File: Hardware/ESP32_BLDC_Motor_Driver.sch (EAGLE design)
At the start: 125 parts, among them J1 USB-C Connector, J2 0532610371, J3 POWER_JACKPOWER_JACK_SLOT, J4 Breadboard Connector, J5 Breadboard Headers, J6 0.1in header, J7 QWIIC_RIGHT_ANGLE, J8 Breakout Header, Q1 20V/4.2A/52mΩ/1.4W, Q2 NPN Transistors, U1 TMC6300, U3 ESP-WROOM-3232D, U4 CH340C, U5 ESD Diode, U6 AP63357, U7 AP2202-ADJ, U8 TMAG5273, U9 LMV324

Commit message: Design review changes
Updated datasheets with correct parts in it now; removed power jack; changed direction of motor and output connector to the motor; swapped resistances of op amp for inline current sensing; updated sizes of some resistances; fixed power scheme of the board; added perfect diode circuit; for more information, see protos review doc
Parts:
- removed C16: 10uF, SparkFun-Capacitors:10UF-0603-6.3V-20%
- removed C20, C21: 22uF, SparkFun-Capacitors:22UF-0603-6.3V-20%
- removed D1: 1A/40V/500mV, SparkFun-DiscreteSemi:DIODE-SCHOTTKY-SS14
- removed J2: 0532610371, 0532610371:0532610371
- removed J3: POWER_JACKPOWER_JACK_SLOT, SparkFun-Connectors:POWER_JACKPOWER_JACK_SLOT
- removed J6: 0.1in header, SparkFun-Connectors:CONN_03
- removed J8: Breakout Header, SparkFun-Connectors:CONN_02
- removed L1: 4.7μH, SparkFun-Coils:4.7μH_SHIELDED_INDUCTORNPIS_LS
- removed MOTOR: JUMPER-SMT_2_NC_TRACE_SILK, SparkFun-Jumpers:JUMPER-SMT_2_NC_TRACE_SILK
- removed MPWR: RED, SparkFun-LED:LED-RED_0603-KB
- removed R22: 16.2k, SparkFun-Resistors:16.2KOHM-0603-1/10W-1%
- removed R23: 26.7k, SparkFun-Resistors:26.7KOHM0603-1/10W-1%
- removed R5: 93.1k, SparkFun-Resistors:93.1KOHM
- removed R6: 30.1k, SparkFun-Resistors:30.1KOHM-0603-1/10W-1%
- removed U6: AP63357, SparkFun-IC-Power:AP63357
- removed U7: AP2202-ADJ, SparkFun-IC-Power:AP2202-ADJ
- added C12: 0.1uF, SparkFun-Capacitors:0.1UF-0603-25V-(+80/-20%)
- added MEAS: JUMPER-COMBO_2_NC_TRACE, SparkFun-Jumpers:JUMPER-COMBO_2_NC_TRACE
- added P1: 0532610371, 0532610371:0532610371
- added Q3: 20V/4.2A/52mΩ/1.4W, SparkFun-DiscreteSemi:MOSFET_PCH-DMG2305UX-7
- added U2: 3.3V, SparkFun-IC-Power:V_REG_AP2112K-3.3V
- C11: value 100pF -> 0.1uF; device SparkFun-Capacitors:100PF-0603-50V-5% -> SparkFun-Capacitors:0.1UF-0603-25V-(+80/-20%)
- C5: value 0.1uF -> 10nF; device SparkFun-Capacitors:0.1UF-0603-25V-(+80/-20%) -> SparkFun-Capacitors:10NF-0603-50V-10%
- C6: value 33pF -> 0.1uF; device SparkFun-Capacitors:33PF-0603-50V-5% -> SparkFun-Capacitors:0.1UF-0603-25V-(+80/-20%)
- C7: device SparkFun-Capacitors:10UF-0603-6.3V-20% -> SparkFun-Capacitors:10UF-POLAR-0603-6.3V-20%(TANT)
- Q1: value 20V/4.2A/52mΩ/1.4W -> (none); device SparkFun-DiscreteSemi:MOSFET_PCH-DMG2305UX-7 -> SparkFun-DiscreteSemi:TRANS_PNP_DUALSOT-363
- R1: value 4.7k -> 100k; device SparkFun-Resistors:4.7KOHM-0603-1/10W-1% -> SparkFun-Resistors:100KOHM-0603-1/10W-1%
- R4: value 100k -> 1M; device SparkFun-Resistors:100KOHM-0603-1/10W-1% -> SparkFun-Resistors:1MOHM-0603-1/4W-5%
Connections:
- removed net 3.3V_A: C1.1, C17.1, C22.1, C4.1, C9.1, J7.2, PWR.2, R16.2, R22.2, STAT.VCC, U3.3V3, U4.V3, U4.VCC, U7.OUT
- removed net 3.3V_PG: J5.1, U6.PG
- removed net BST: C5.1, U6.BST
- removed net ESP_13/U_OUT: R35.2, TP10.1, U3.PICO2/IOA13, U9G2.OUT
- removed net ESP_14/DIAG: D.2, U1.DIAG, U3.SCK2/IOA14
- removed net ESP_34/AUX1: J5.7, S3.1, S3.2, U3.IA34
- removed net ESP_35/AUX2: J5.8, S4.1, S4.2, U3.IA35
- removed net FB: C6.2, R5.1, R6.2, U6.FB
- removed net LDO_EN: R24.1, U7.EN
- removed net MOTOR_EN: J4.6, U6.EN
- removed net N$23: MOTOR.1, R1.2
- removed net N$34: MPWR.A, R1.1
- removed net N$5: J3.GNDBREAK, Q1.G, R4.1
- removed net POWER_IN: D1.A, J3.PWR
- removed net SW: C5.2, L1.1, U6.SW
- removed net VIN: C10.1, C16.1, C7.1, D1.C, J8.2, Q1.S, R24.2, R4.2, U6.VIN, U7.IN
- new net 5V: BYP.2, C10.1, C12.1, F1.2, R24.2, U2.IN
- new net 5V_MEAS: MEAS.1, Q1G2.E, Q3.S
- new net ESP_13/AUX2: J5.8, S4.1, S4.2, U3.PICO2/IOA13
- new net ESP_14/AUX1: J5.7, S3.1, S3.2, U3.SCK2/IOA14
- new net ESP_21/TP_SDA1: R27.1
- new net ESP_34/DIAG: D.2, U1.DIAG, U3.IA34
- new net ESP_35/U_OUT: R29.2, TP10.1, U3.IA35, U9G2.OUT
- new net N$21: Q1G2.C, Q3.G, R4.2
- new net N$22: Q1G1.B, Q1G1.E, Q1G2.B, R1.2
- new net N$6: R24.1, U2.EN
- net 3.3V: now also C1.1, C17.1, C22.1, C4.1, C9.1, J7.2, PWR.2, R16.2, STAT.VCC, U2.OUT, U3.3V3, U4.VCC; no longer C20.1, C21.1, C6.1, L1.2, MOTOR.2, R5.2
- net ESP_21/TP_SDA: now also J4.3; no longer J4.2, R27.1
- net ESP_22/TP_SCL: now also J4.2; no longer J4.1
- net ESP_25/TP_A1: now also J4.6; no longer J4.5
- net ESP_26/TP_A0: now also J4.5; no longer J4.4
- net ESP_27/GPIO2: now also J4.4; no longer J4.3
- net ESP_36/V_OUT: now also R40.2; no longer R36.2
- net ESP_39/W_OUT: now also R41.2; no longer R37.2
- net GND: now also C12.2, C5.2, C6.2, C7.-, J4.1, J5.1, R1.1, R30.2, R4.1, R42.2, R43.2, U2.GND; no longer C16.2, C20.2, C21.2, C7.2, J3.GND, J8.1, MPWR.C, R23.1, R31.2, R38.2, R39.2, R6.1, U6.COMP, U6.GND, U7.GND
- net N$16: now also R29.1, R35.2; no longer R29.2, R35.1
- net N$17: now also C11.1, MEAS.2; no longer J1.VBUS
- net N$18: now also R30.1, R31.2; no longer R30.2, R31.1
- net N$19: now also R36.2, R40.1; no longer R36.1, R40.2
- net N$2: now also C5.1, U4.V3; no longer C11.1, R22.1, R23.2, U7.ADJ
- net N$20: now also R38.2, R43.1; no longer R38.1, R43.2
- net N$24: now also R37.2, R41.1; no longer R37.1, R41.2
- net N$25: now also R39.2, R42.1; no longer R39.1, R42.2
- net SENSE_U: now also R31.1; no longer R30.1
- net SENSE_V: now also R38.1; no longer R43.1
- net SENSE_W: now also R39.1; no longer R42.1
- net U: now also P1.3, R35.1; no longer J2.3, J6.3, R29.1
- net V: now also P1.2, R36.1; no longer J2.2, J6.2, R40.1
- net V_USB: now also C6.1, C7.+, J1.VBUS, Q1G1.C, Q3.D; no longer BYP.2, F1.2, Q1.D
- net W: now also P1.1, R37.1; no longer J2.1, J6.1, R41.1
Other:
- note added: "3.3V Regulator"
- note added: "5V Bus Perfect Diodes"
- note added: "Current Measure Header and Fuse Jumper"
- note added: "I2C Pullups"
- note removed: "20V/4.2A/1.4W"
- note removed: "3.3V_A is the alternate voltage supply on board"
- note removed: "Breakout headers for use case of user choosing a different power connection other than USB or Power Jack"
- note removed: "Cut Jumper MOTOR to disable Motor Power LED"
- note removed: "MPWR"
- note removed: "Motor Power Supply"
- note removed: "Power Supply - LDO"
- note removed: "Vin Range: 4V - 15V"
- moved on the sheet: BYP, C1, C10, C11, C17, C18, C19, C2, C22, C23, C3, C4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

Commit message: Design Review Changes
Added back in AP63557 circuit for more power to motor; Adjusted trace size for better differential pairs and power usage; created standoff board for the motor to sit on while moving; see design notes for more information.
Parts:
- removed LOGO5: SFE_LOGO_NAME.1_INCH, SparkFun-Aesthetics:SFE_LOGO_NAME.1_INCH
- added C13, C14: 10uF, SparkFun-Capacitors:10UF-0603-6.3V-20%
- added C15: 0.1uF, SparkFun-Capacitors:0.1UF-0603-25V-5%
- added C16: 33pF, SparkFun-Capacitors:33PF-0603-50V-5%
- added C20, C21: 22uF, SparkFun-Capacitors:22UF-0603-6.3V-20%
- added D1: RED, SparkFun-LED:LED-RED_0603-KB
- added L1: 4.7μH, SparkFun-Coils:4.7μH_SHIELDED_INDUCTORNPIS_LS
- added MPWR: JUMPER-SMT_2_NC_TRACE_SILK, SparkFun-Jumpers:JUMPER-SMT_2_NC_TRACE_SILK
- added R22: 4.7k, SparkFun-Resistors:4.7KOHM-0603-1/10W-1%
- added R5: 93.1k, SparkFun-Resistors:93.1KOHM
- added R6: 30.1k, SparkFun-Resistors:30.1KOHM-0603-1/10W-1%
- added U6: AP63357, SparkFun-IC-Power:AP63357
- renumbered D to DIAG, S to !STBY
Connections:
- removed net ESP_21/TP_SDA1: R27.1
- new net 3.3V_A: C16.2, C18.1, C19.1, C2.1, C20.1, C21.1, C3.1, D7.C, L1.2, MPWR.2, R5.2, U1.VS, U9G5.P$V+
- new net 3.3V_PG: U6.PG
- new net BST: C15.1, U6.BST
- new net FB: C16.1, R5.1, R6.2, U6.FB
- new net MOTOR_EN: J5.1, U6.EN
- new net N$26: D1.A, R22.1
- new net N$27: MPWR.1, R22.2
- new net SW: C15.2, L1.1, U6.SW
- net 3.3V: no longer C18.1, C19.1, C2.1, C3.1, D7.C, U1.VS, U9G5.P$V+
- net 5V: now also C13.1, C14.1, U6.VIN
- net ESP_21/TP_SDA: now also R27.1
- net GND: now also C13.2, C14.2, C20.2, C21.2, D1.C, R6.1, U6.COMP, U6.GND; no longer J5.1
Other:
- note added: "3.3V_A is the alternate voltage that is used for the motor driver"
- note added: "Cut Jumper DIAG to disable diagnostic LED"
- note added: "Cut Jumper MPWR to disable Motor Power LED"
- note added: "Cut Jumper STBY to disable standby LED"
- note added: "Input Range: 4V to 6V Output Current: 600mA MAX"
- note added: "Input Range: 6V to 32V Output Current: 3.5A MAX"
- note added: "Motor Voltage Regulator"
- note removed: "Cut Jumper D to disable diagnostic LED"
- note removed: "Cut Jumper S to disable standby LED"
- moved on the sheet: BYP, C1, C10, C11, C12, C17, C22, C23, C4, C5, C6, C7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

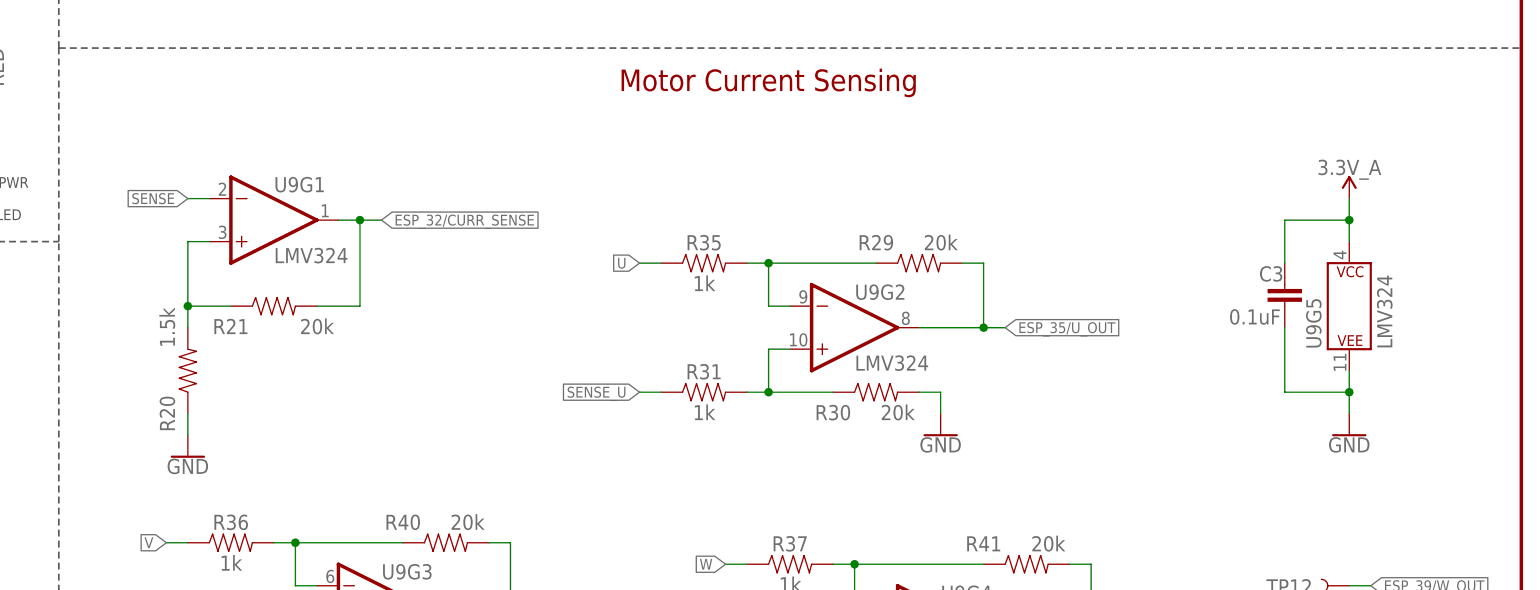
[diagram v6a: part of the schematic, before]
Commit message: Final design changes made; files for ordering added
Made final adjustments with Alex - check document for more information on small adjustments; ran CAM script for output files for board; also made output CAM files for standoff to be ordered as well.
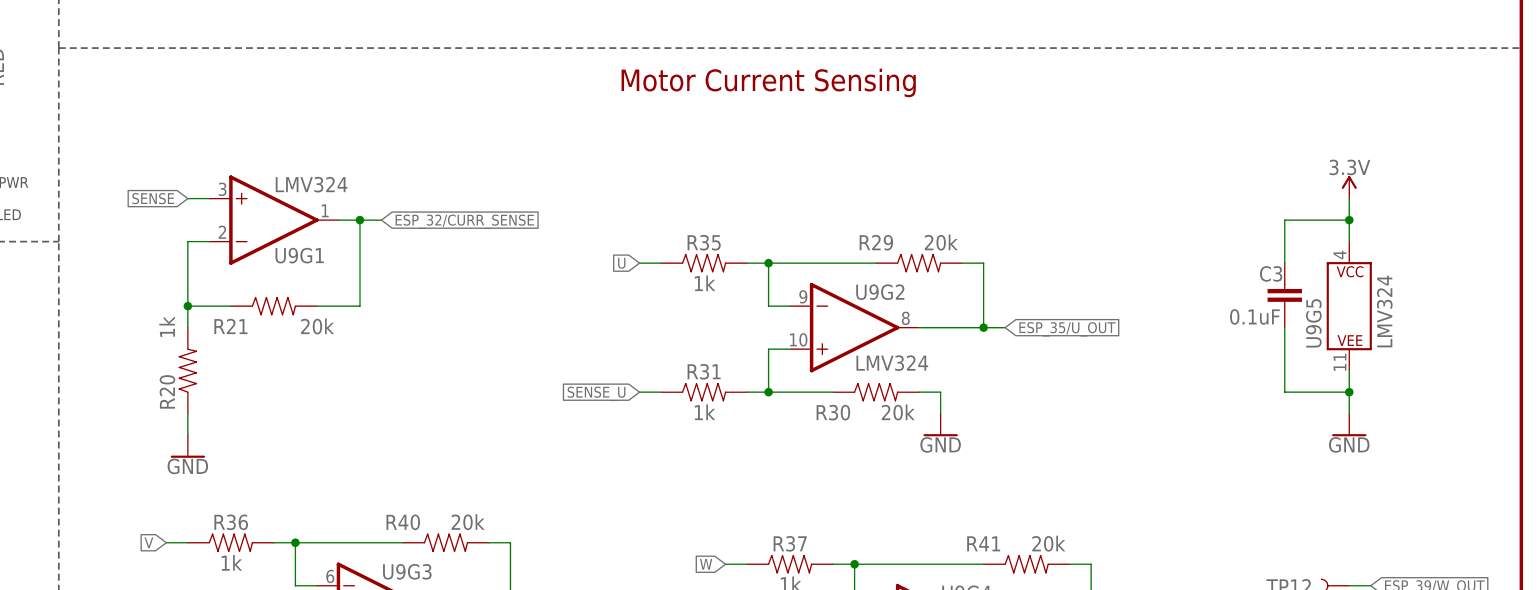
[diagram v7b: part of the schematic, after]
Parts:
- R20: value 1.5k -> 1k; device SparkFun-Resistors:1.5KOHM-0603-1/10W-1% -> SparkFun-Resistors:1KOHM-0603-1/10W-1%
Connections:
- net 3.3V: now also C3.1, U9G5.P$V+
- net 3.3V_A: no longer C3.1, U9G5.P$V+
- net N$14: now also U9G1.-IN; no longer U9G1.+IN
- net SENSE: now also U9G1.+IN; no longer U9G1.-IN
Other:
- moved on the sheet: U9G1
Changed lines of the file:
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@@
 <part name="U9" library="SparkFun-IC-Amplifiers" deviceset="LMV324" device="" value="LMV324"/>
 <part name="R21" library="SparkFun-Resistors" deviceset="20KOHM" device="-0603-1/10W-1%" value="20k"/>
-<part name="R20" library="SparkFun-Resistors" deviceset="1.5KOHM" device="-0603-1/10W-1%" value="1.5k"/>
 <part name="GND15" library="SparkFun-PowerSymbols" deviceset="GND" device=""/>
 <part name="C3" library="SparkFun-Capacitors" deviceset="0.1UF" device="-0603-25V-10%-X7R-WE" value="0.1uF"/>
@@
 <part name="D1" library="SparkFun-LED" deviceset="LED-RED" device="_0603-KB" value="RED"/>
 <part name="SUPPLY26" library="SparkFun-PowerSymbols" deviceset="3.3V_A" device=""/>
-<part name="SUPPLY2" library="SparkFun-PowerSymbols" deviceset="3.3V_A" device=""/>
 <part name="SUPPLY3" library="SparkFun-PowerSymbols" deviceset="3.3V_A" device=""/>
 <part name="SUPPLY8" library="SparkFun-PowerSymbols" deviceset="3.3V_A" device=""/>
 <part name="SUPPLY17" library="SparkFun-PowerSymbols" deviceset="3.3V_A" device=""/>
 <part name="SUPPLY24" library="SparkFun-PowerSymbols" deviceset="3.3V_A" device=""/>
+<part name="R20" library="SparkFun-Resistors" deviceset="1KOHM" device="-0603-1/10W-1%" value="1k"/>
+<part name="SUPPLY2" library="SparkFun-PowerSymbols" deviceset="3.3V" device=""/>
 </parts>
 <sheets>
@@
 <attribute name="VALUE" x="289.56" y="135.636" size="1.778" layer="96" font="vector" align="top-center"/>
 </instance>
-<instance part="R20" gate="G$1" x="274.32" y="129.54" smashed="yes" rot="R90">
-<attribute name="NAME" x="272.796" y="124.46" size="1.778" layer="95" font="vector" rot="R90" align="bottom-center"/>
-<attribute name="VALUE" x="272.796" y="134.62" size="1.778" layer="96" font="vector" rot="R270" align="top-center"/>
-</instance>
 <instance part="GND15" gate="1" x="274.32" y="119.38" smashed="yes">
 <attribute name="VALUE" x="274.32" y="119.126" size="1.778" layer="96" font="vector" align="top-center"/>
@@
 <attribute name="VALUE" x="381" y="86.106" size="1.778" layer="96" font="vector" align="top-center"/>
 </instance>
-<instance part="U9" gate="G1" x="284.48" y="147.32" smashed="yes">
-<attribute name="NAME" x="284.48" y="150.622" size="1.778" layer="95" font="vector"/>
-<attribute name="VALUE" x="284.48" y="142.24" size="1.778" layer="95" font="vector"/>
+<instance part="U9" gate="G1" x="284.48" y="147.32" smashed="yes" rot="MR180">
+<attribute name="NAME" x="284.48" y="144.018" size="1.778" layer="95" font="vector" rot="MR180"/>
+<attribute name="VALUE" x="284.48" y="152.4" size="1.778" layer="95" font="vector" rot="MR180"/>
 </instance>
 <instance part="U9" gate="G2" x="353.06" y="134.62" smashed="yes">
@@
 <attribute name="VALUE" x="248.92" y="200.914" size="1.778" layer="96" font="vector" align="bottom-center"/>
 </instance>
+<instance part="SUPPLY3" gate="G$1" x="322.58" y="248.92" smashed="yes">
+<attribute name="VALUE" x="322.58" y="251.714" size="1.778" layer="96" font="vector" align="bottom-center"/>
+</instance>
+<instance part="SUPPLY8" gate="G$1" x="287.02" y="264.16" smashed="yes">
+<attribute name="VALUE" x="287.02" y="266.954" size="1.778" layer="96" font="vector" align="bottom-center"/>
+</instance>
+<instance part="SUPPLY17" gate="G$1" x="297.18" y="264.16" smashed="yes">
+<attribute name="VALUE" x="297.18" y="266.954" size="1.778" layer="96" font="vector" align="bottom-center"/>
+</instance>
+<instance part="SUPPLY24" gate="G$1" x="307.34" y="264.16" smashed="yes">
+<attribute name="VALUE" x="307.34" y="266.954" size="1.778" layer="96" font="vector" align="bottom-center"/>
+</instance>
+<instance part="R20" gate="G$1" x="274.32" y="129.54" smashed="yes" rot="R90">
+<attribute name="NAME" x="272.796" y="127" size="1.778" layer="95" font="vector" rot="R90" align="bottom-center"/>
+<attribute name="VALUE" x="272.796" y="134.62" size="1.778" layer="96" font="vector" rot="R270" align="top-center"/>
+</instance>
 <instance part="SUPPLY2" gate="G$1" x="411.48" y="149.86" smashed="yes">
 <attribute name="VALUE" x="411.48" y="152.654" size="1.778" layer="96" font="vector" align="bottom-center"/>
-</instance>
-<instance part="SUPPLY3" gate="G$1" x="322.58" y="248.92" smashed="yes">
-<attribute name="VALUE" x="322.58" y="251.714" size="1.778" layer="96" font="vector" align="bottom-center"/>
-</instance>
-<instance part="SUPPLY8" gate="G$1" x="287.02" y="264.16" smashed="yes">
-<attribute name="VALUE" x="287.02" y="266.954" size="1.778" layer="96" font="vector" align="bottom-center"/>
-</instance>
-<instance part="SUPPLY17" gate="G$1" x="297.18" y="264.16" smashed="yes">
-<attribute name="VALUE" x="297.18" y="266.954" size="1.778" layer="96" font="vector" align="bottom-center"/>
-</instance>
-<instance part="SUPPLY24" gate="G$1" x="307.34" y="264.16" smashed="yes">
-<attribute name="VALUE" x="307.34" y="266.954" size="1.778" layer="96" font="vector" align="bottom-center"/>
 </instance>
 </instances>
@@
 <wire x1="313.944" y1="27.432" x2="313.944" y2="29.972" width="0.1524" layer="91"/>
 <pinref part="SUPPLY21" gate="G$1" pin="3.3V"/>
+</segment>
+<segment>
+<pinref part="U9" gate="G5" pin="P$V+"/>
+<wire x1="411.48" y1="144.78" x2="411.48" y2="147.32" width="0.1524" layer="91"/>
+<wire x1="411.48" y1="147.32" x2="411.48" y2="149.86" width="0.1524" layer="91"/>
+<wire x1="411.48" y1="147.32" x2="403.86" y2="147.32" width="0.1524" layer="91"/>
+<junction x="411.48" y="147.32"/>
+<wire x1="403.86" y1="147.32" x2="403.86" y2="142.24" width="0.1524" layer="91"/>
+<pinref part="C3" gate="G$1" pin="1"/>
+<pinref part="SUPPLY2" gate="G$1" pin="3.3V"/>
 </segment>
 </net>
@@
 </segment>
 <segment>
+<pinref part="U9" gate="G1" pin="+IN"/>
 <wire x1="276.86" y1="149.86" x2="274.32" y2="149.86" width="0.1524" layer="91"/>
 <label x="274.32" y="149.86" size="1.27" layer="95" font="vector" rot="R180" xref="yes"/>
-<pinref part="U9" gate="G1" pin="-IN"/>
 </segment>
 </net>
@@
 </segment>
 <segment>
-<wire x1="292.1" y1="147.32" x2="294.64" y2="147.32" width="0.1524" layer="91"/>
 <wire x1="294.64" y1="147.32" x2="294.64" y2="137.16" width="0.1524" layer="91"/>
 <wire x1="294.64" y1="147.32" x2="297.18" y2="147.32" width="0.1524" layer="91"/>
-<junction x="294.64" y="147.32"/>
 <pinref part="R21" gate="G$1" pin="2"/>
 <wire x1="289.56" y1="137.16" x2="294.64" y2="137.16" width="0.1524" layer="91"/>
 <label x="297.18" y="147.32" size="1.27" layer="95" font="vector" xref="yes"/>
 <pinref part="U9" gate="G1" pin="OUT"/>
+<wire x1="292.1" y1="147.32" x2="294.64" y2="147.32" width="0.1524" layer="91"/>
+<junction x="294.64" y="147.32"/>
 </segment>
 </net>
 <net name="N$14" class="0">
 <segment>
-<wire x1="276.86" y1="144.78" x2="274.32" y2="144.78" width="0.1524" layer="91"/>
 <wire x1="274.32" y1="144.78" x2="274.32" y2="137.16" width="0.1524" layer="91"/>
 <wire x1="274.32" y1="137.16" x2="279.4" y2="137.16" width="0.1524" layer="91"/>
@@
 <junction x="274.32" y="137.16"/>
 <pinref part="R20" gate="G$1" pin="2"/>
-<pinref part="U9" gate="G1" pin="+IN"/>
+<pinref part="U9" gate="G1" pin="-IN"/>
+<wire x1="274.32" y1="144.78" x2="276.86" y2="144.78" width="0.1524" layer="91"/>
 </segment>
 </net>
@@
 </segment>
 <segment>
-<pinref part="U9" gate="G5" pin="P$V+"/>
-<wire x1="411.48" y1="144.78" x2="411.48" y2="147.32" width="0.1524" layer="91"/>
-<wire x1="411.48" y1="147.32" x2="411.48" y2="149.86" width="0.1524" layer="91"/>
-<wire x1="411.48" y1="147.32" x2="403.86" y2="147.32" width="0.1524" layer="91"/>
-<junction x="411.48" y="147.32"/>
-<wire x1="403.86" y1="147.32" x2="403.86" y2="142.24" width="0.1524" layer="91"/>
-<pinref part="C3" gate="G$1" pin="1"/>
-<pinref part="SUPPLY2" gate="G$1" pin="3.3V_A"/>
-</segment>
-<segment>
